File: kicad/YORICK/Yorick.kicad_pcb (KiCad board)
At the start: 2 copper layers, 124 x 112 mm, 64 parts, among them J1 Conn_01x12, J2 AVR-ISP-6, J3 AudioJack2_SwitchT, J4 USB_B_Micro, J5 AudioJack2_SwitchT, Q1 Q_NJFET_DSG, Q2 Q_NJFET_DSG, SW1 SW_Push, SW2 SW_Push, U1 4069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

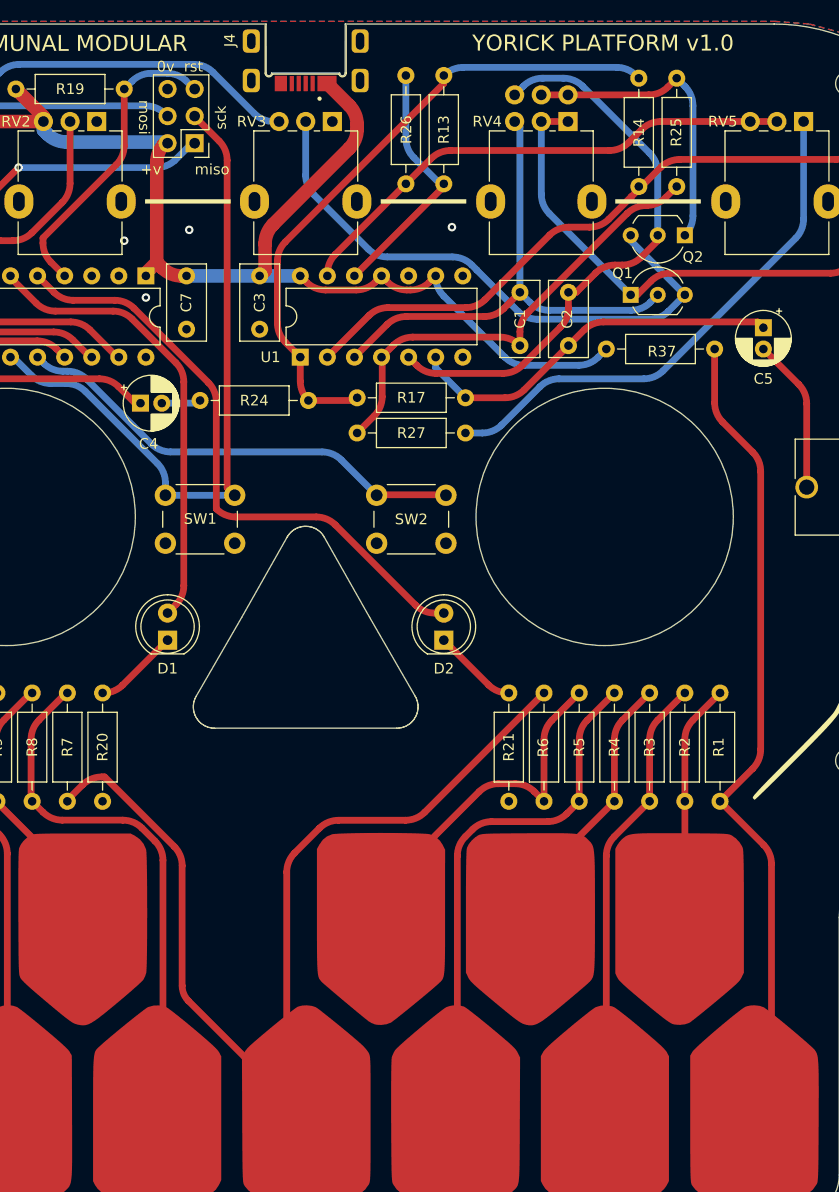
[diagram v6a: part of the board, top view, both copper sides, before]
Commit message: Adding copper keepout around teeth
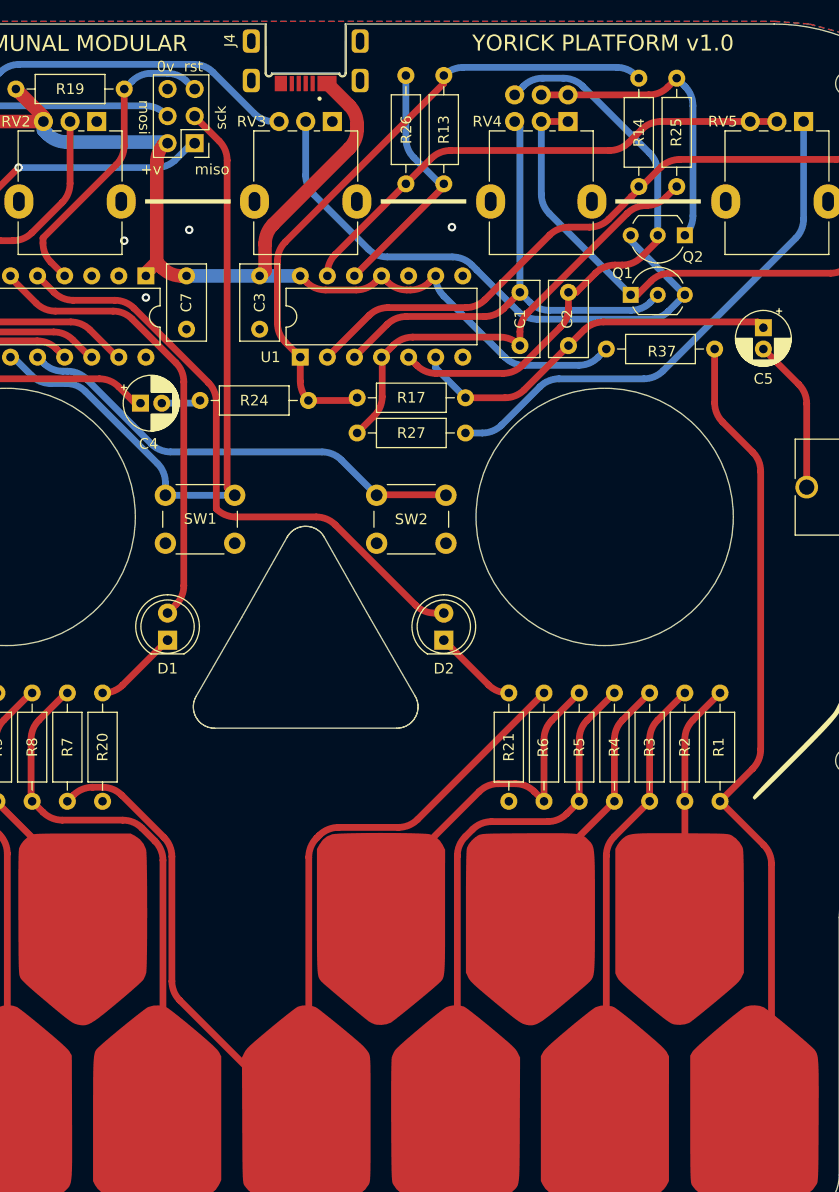
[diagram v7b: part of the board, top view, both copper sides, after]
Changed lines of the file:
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@@
       (drillshape 0)
       (scaleselection 1)
-      (outputdirectory "../gerbers/")
+      (outputdirectory "../../gerbers/")
     )
   )
@@
   (gr_line (start 162.270226 108.263801) (end 162.09513 108.516652)
     (stroke (width 0.1) (type default)) (layer "Edge.Cuts"))
-  (gr_line (start 105.3084 35.56) (end 145.546 35.56)
+  (gr_line (start 105.3084 35.56) (end 145.542 35.56)
     (stroke (width 0.1) (type default)) (layer "Edge.Cuts"))
   (gr_line (start 48.357102 112.941035) (end 47.842022 112.589879)
@@
   (arc (start 88.2144 113.99088) (mid 88.021054 113.018864) (end 87.470451 112.194829) (width 0.635) (layer "F.Cu") (net 17))
   (arc (start 78.76581 110.225708) (mid 77.793794 110.032362) (end 76.969759 109.481759) (width 0.635) (layer "F.Cu") (net 17))
-  (segment (start 102.888051 110.979949) (end 100.565949 113.302051) (width 0.635) (layer "F.Cu") (net 18))
-  (segment (start 79.248 108.346108) (end 80.678159 106.915949) (width 0.635) (layer "F.Cu") (net 18))
-  (segment (start 110.961898 110.236) (end 104.684102 110.236) (width 0.635) (layer "F.Cu") (net 18))
-  (segment (start 90.600187 127.177495) (end 101.888252 138.46556) (width 0.635) (layer "F.Cu") (net 18))
-  (segment (start 82.47421 106.172) (end 82.746265 106.172) (width 0.635) (layer "F.Cu") (net 18))
-  (segment (start 99.822 115.098102) (end 99.822 136.738748) (width 0.635) (layer "F.Cu") (net 18))
-  (segment (start 90.0144 114.492237) (end 90.0144 125.763281) (width 0.635) (layer "F.Cu") (net 18))
-  (segment (start 123.952 98.298) (end 112.757949 109.492051) (width 0.635) (layer "F.Cu") (net 18))
-  (segment (start 82.746265 106.172) (end 89.270451 112.696186) (width 0.635) (layer "F.Cu") (net 18))
-  (arc (start 89.270451 112.696186) (mid 89.821054 113.520221) (end 90.0144 114.492237) (width 0.635) (layer "F.Cu") (net 18))
-  (arc (start 100.565949 113.302051) (mid 100.015346 114.126086) (end 99.822 115.098102) (width 0.635) (layer "F.Cu") (net 18))
-  (arc (start 80.678159 106.915949) (mid 81.502194 106.365346) (end 82.47421 106.172) (width 0.635) (layer "F.Cu") (net 18))
-  (arc (start 104.684102 110.236) (mid 103.712086 110.429346) (end 102.888051 110.979949) (width 0.635) (layer "F.Cu") (net 18))
-  (arc (start 110.961898 110.236) (mid 111.933914 110.042654) (end 112.757949 109.492051) (width 0.635) (layer "F.Cu") (net 18))
-  (arc (start 90.0144 125.763281) (mid 90.166641 126.528647) (end 90.600187 127.177495) (width 0.635) (layer "F.Cu") (net 18))
+  (segment (start 79.248 108.458) (end 79.824751 107.881249) (width 0.635) (layer "F.Cu") (net 18))
+  (segment (start 101.888252 113.695843) (end 101.888252 138.805) (width 0.635) (layer "F.Cu") (net 18))
+  (segment (start 89.0526 113.643686) (end 89.0526 125.338498) (width 0.635) (layer "F.Cu") (net 18))
+  (segment (start 102.882688 111.649305) (end 102.632201 111.899792) (width 0.635) (layer "F.Cu") (net 18))
+  (segment (start 89.796549 127.134549) (end 101.467 138.805) (width 0.635) (layer "F.Cu") (net 18))
+  (segment (start 110.292542 110.905356) (end 104.678739 110.905356) (width 0.635) (layer "F.Cu") (net 18))
+  (segment (start 81.620802 107.1373) (end 82.546214 107.1373) (width 0.635) (layer "F.Cu") (net 18))
+  (segment (start 123.952 98.298) (end 112.088593 110.161407) (width 0.635) (layer "F.Cu") (net 18))
+  (segment (start 84.342265 107.881249) (end 88.308651 111.847635) (width 0.635) (layer "F.Cu") (net 18))
+  (segment (start 101.467 138.805) (end 101.888252 138.805) (width 0.635) (layer "F.Cu") (net 18))
+  (arc (start 88.308651 111.847635) (mid 88.859254 112.67167) (end 89.0526 113.643686) (width 0.635) (layer "F.Cu") (net 18))
+  (arc (start 104.678739 110.905356) (mid 103.706723 111.098702) (end 102.882688 111.649305) (width 0.635) (layer "F.Cu") (net 18))
+  (arc (start 81.620802 107.1373) (mid 80.648786 107.330646) (end 79.824751 107.881249) (width 0.635) (layer "F.Cu") (net 18))
+  (arc (start 110.292542 110.905356) (mid 111.264558 110.71201) (end 112.088593 110.161407) (width 0.635) (layer "F.Cu") (net 18))
+  (arc (start 102.632201 111.899792) (mid 102.081598 112.723827) (end 101.888252 113.695843) (width 0.635) (layer "F.Cu") (net 18))
+  (arc (start 89.796549 127.134549) (mid 89.245946 126.310514) (end 89.0526 125.338498) (width 0.635) (layer "F.Cu") (net 18))
+  (arc (start 82.546214 107.1373) (mid 83.51823 107.330646) (end 84.342265 107.881249) (width 0.635) (layer "F.Cu") (net 18))
   (segment (start 121.248898 106.807) (end 119.670102 106.807) (width 0.635) (layer "F.Cu") (net 19))
   (segment (start 117.874051 107.550949) (end 106.638252 118.786748) (width 0.635) (layer "F.Cu") (net 19))
@@
   (segment (start 57.15 66.802) (end 57.15 66.584102) (width 0.635) (layer "B.Cu") (net 53))
   (arc (start 57.893949 64.788051) (mid 57.343346 65.612086) (end 57.15 66.584102) (width 0.635) (layer "B.Cu") (net 53))
+  (zone (net 0) (net_name "") (layer "F.Cu") (hatch edge 0.5)
+    (connect_pads (clearance 0))
+    (min_thickness 0.25) (filled_areas_thickness no)
+    (keepout (tracks allowed) (vias allowed) (pads allowed) (copperpour not_allowed) (footprints allowed))
+    (fill (thermal_gap 0.5) (thermal_bridge_width 0.5))
+    (polygon
+      (pts
+        (xy 41.783 111.506)
+        (xy 160.401 111.506)
+        (xy 151.892 118.11)
+        (xy 152.019 148.209)
+        (xy 50.8 148.336)
+        (xy 49.657 117.221)
+      )
+    )
+  )
   (zone (net 6) (net_name "GND") (layers "F&B.Cu") (hatch edge 0.5)
     (connect_pads (clearance 0.5))
